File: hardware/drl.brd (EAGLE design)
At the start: 60.6 x 32.4 mm, 17 parts, among them IC1 TINY13-20SU, IC3 REG1117, Q1 IRF3205Z, Q2 IRF3205Z, T1 BC817-40, X1 CON1, X2 CON2

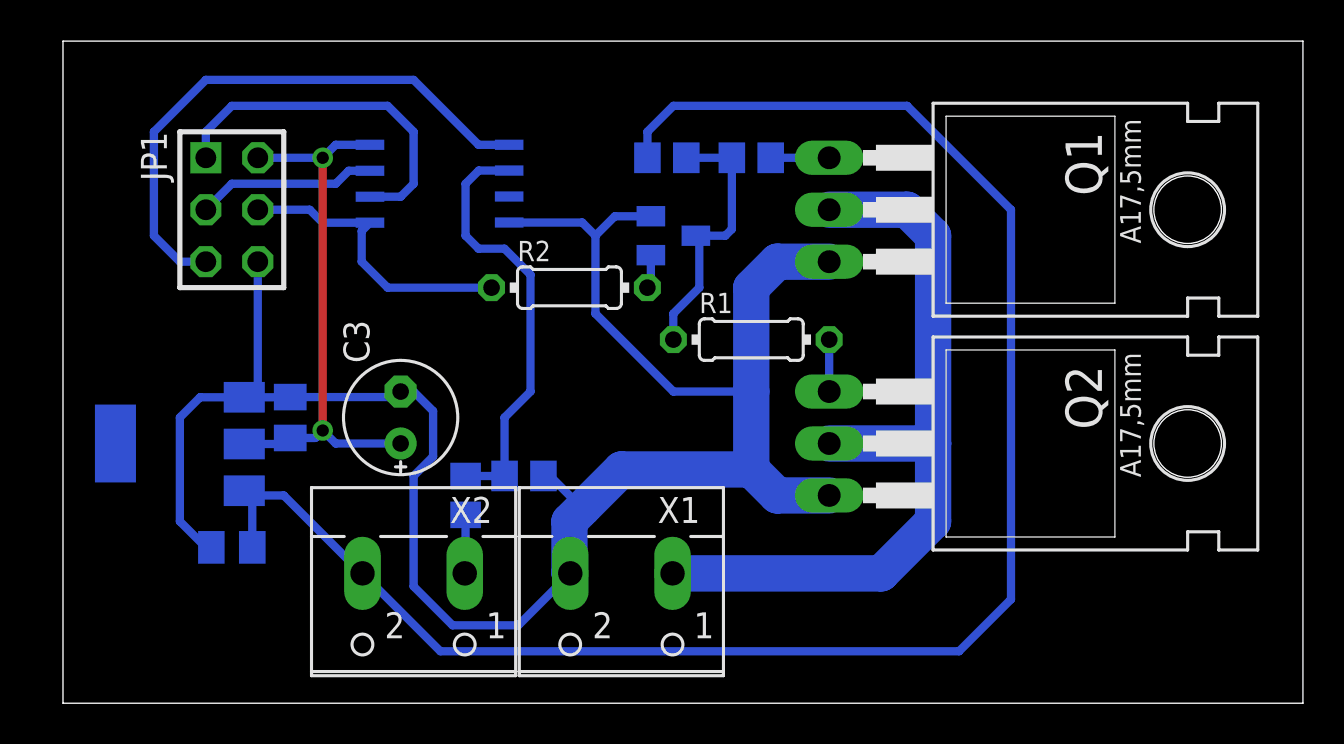
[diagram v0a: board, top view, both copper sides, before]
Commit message: Made the board slightly shorter. More compact component placement.
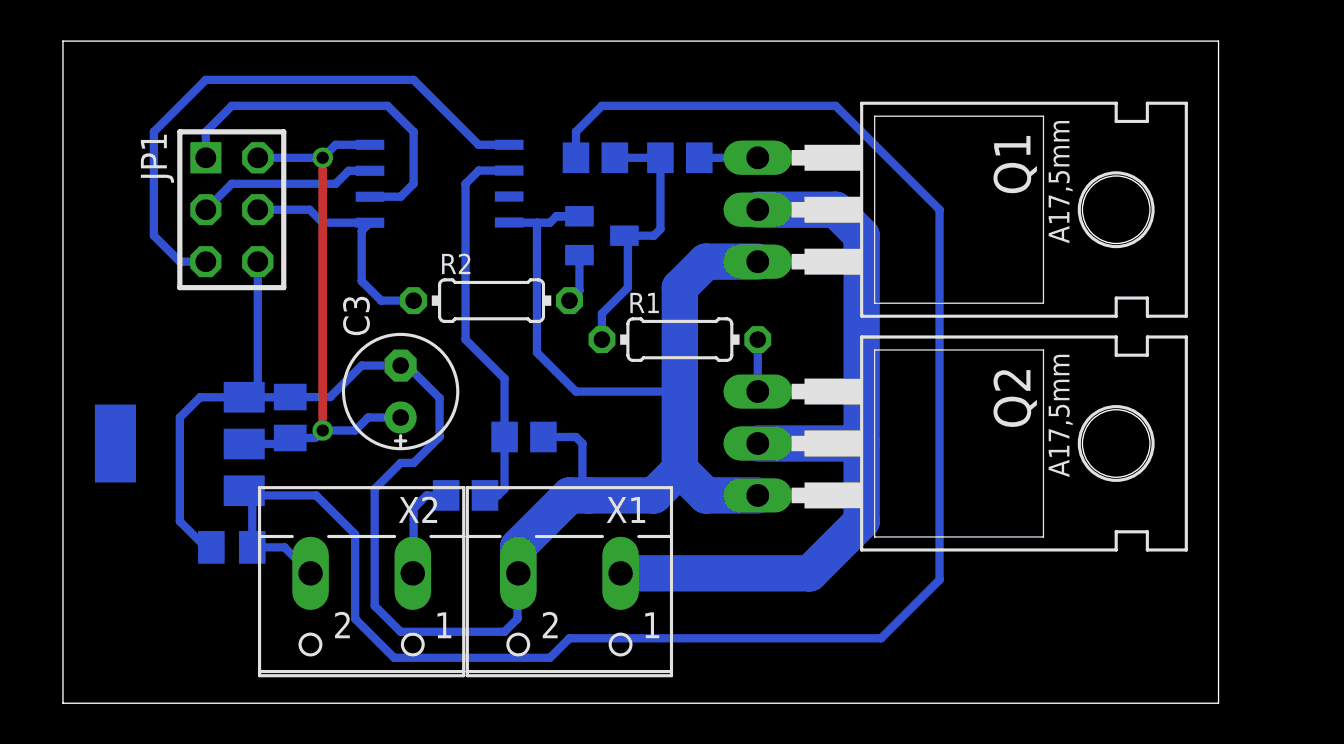
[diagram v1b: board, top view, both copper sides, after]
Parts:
- moved R2 3.86 mm to (21.0, 19.7)
- moved Q1 3.49 mm to (40.3, 24.1)
- moved Q2 3.49 mm to (40.3, 12.7)
- moved R1 3.49 mm to (30.2, 17.8)
- moved R3 3.49 mm to (30.2, 26.7)
- moved R4 3.49 mm to (26.0, 26.7)
- moved T1 3.49 mm to (26.4, 22.9)
- moved X1 2.54 mm to (24.8, 5.08)
- moved X2 2.54 mm to (14.6, 5.08)
- moved R7 1.90 mm to (22.5, 13.0)
- moved C3 1.27 mm to (16.5, 15.2)
- turned R6 to 0 degrees
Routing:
- net N$7: track 14.7 -> 11.7 mm
- net GND: track 99.2 -> 101.9 mm
- net LO_BEAM: track 2.88 -> 5.04 mm
- net +12: track 85.0 -> 87.0 mm
- net N$9: track 21.2 -> 19.2 mm
- net HI_BEAM: track 38.4 -> 37.5 mm
- net N$6: track 1.66 -> 2.43 mm
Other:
- board size 60.6 x 32.4 mm -> 56.5 x 32.4 mm

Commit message: Added ground plane
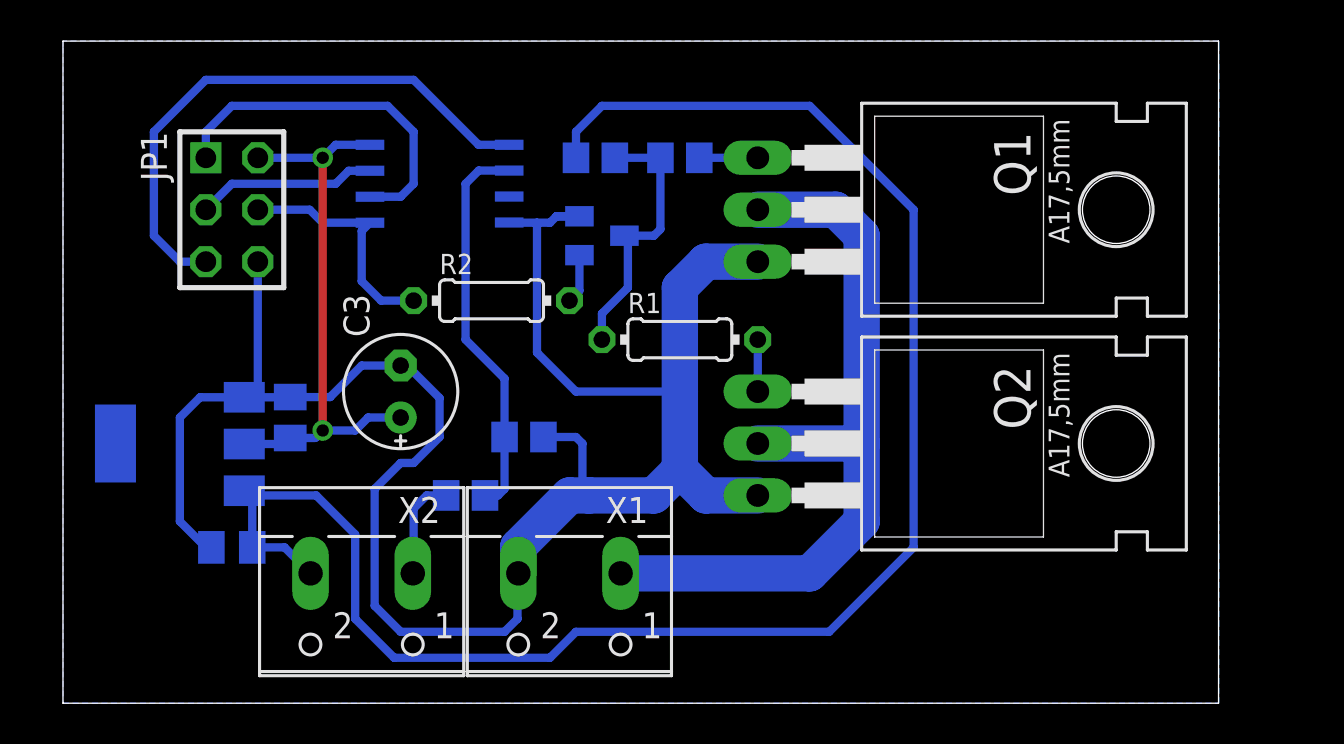
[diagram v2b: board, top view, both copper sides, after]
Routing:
- net +12: track 87.0 -> 83.6 mm
- added copper zone on layer 16, net N$2
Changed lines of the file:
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@@
 <wire x1="25.085" y1="26.67" x2="25.085" y2="27.9425" width="0.4064" layer="16"/>
 <wire x1="25.085" y1="27.9425" x2="26.3525" y2="29.21" width="0.4064" layer="16"/>
-<wire x1="26.3525" y1="29.21" x2="37.7825" y2="29.21" width="0.4064" layer="16"/>
-<wire x1="37.7825" y1="29.21" x2="42.8625" y2="24.13" width="0.4064" layer="16"/>
 <wire x1="9.255" y1="7.62" x2="10.835" y2="7.62" width="0.4064" layer="16"/>
 <wire x1="10.835" y1="7.62" x2="12.105" y2="6.35" width="0.4064" layer="16"/>
-<wire x1="40.005" y1="3.175" x2="42.8625" y2="6.0325" width="0.4064" layer="16"/>
-<wire x1="42.8625" y1="6.0325" x2="42.8625" y2="24.13" width="0.4064" layer="16"/>
 <wire x1="12.3825" y1="10.16" x2="14.2875" y2="8.255" width="0.4064" layer="16"/>
 <wire x1="14.2875" y1="8.255" x2="14.2875" y2="4.1275" width="0.4064" layer="16"/>
 <wire x1="14.2875" y1="4.1275" x2="16.1925" y2="2.2225" width="0.4064" layer="16"/>
 <wire x1="16.1925" y1="2.2225" x2="23.8125" y2="2.2225" width="0.4064" layer="16"/>
-<wire x1="23.8125" y1="2.2225" x2="24.765" y2="3.175" width="0.4064" layer="16"/>
-<wire x1="24.765" y1="3.175" x2="40.005" y2="3.175" width="0.4064" layer="16"/>
+<wire x1="23.8125" y1="2.2225" x2="25.0825" y2="3.4925" width="0.4064" layer="16"/>
+<wire x1="26.3525" y1="29.21" x2="36.5125" y2="29.21" width="0.4064" layer="16"/>
+<wire x1="36.5125" y1="29.21" x2="41.5925" y2="24.13" width="0.4064" layer="16"/>
+<wire x1="41.5925" y1="24.13" x2="41.5925" y2="7.62" width="0.4064" layer="16"/>
+<wire x1="41.5925" y1="7.62" x2="37.465" y2="3.4925" width="0.4064" layer="16"/>
+<wire x1="37.465" y1="3.4925" x2="25.0825" y2="3.4925" width="0.4064" layer="16"/>
 </signal>
 <signal name="N$4">
@@
 <wire x1="17.145" y1="6.39" x2="17.105" y2="6.35" width="0.4064" layer="16"/>
 </signal>
+<signal name="N$2">
+<polygon width="0.4064" layer="16" isolate="0.8128">
+<vertex x="0" y="0"/>
+<vertex x="56.515" y="0"/>
+<vertex x="56.515" y="32.0675"/>
+<vertex x="56.515" y="32.385"/>
+<vertex x="0" y="32.385"/>
+<vertex x="0" y="32.0675"/>
+</polygon>
+</signal>
 </signals>

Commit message: Change in schematic and board.
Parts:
- added C4: 47u, rcl:E2,5-6E
- added D1: (no value), semicon-smd-ipc:SOD80
- added R5: 10k, rcl:R0805
- C3: value 22u -> 100u
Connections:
- new net VCC12: C1.1, C4.+, D1.1, IC3.3, R4.2
- net +12: now also D1.2; no longer C1.1, IC3.3, R4.2
- net GND: now also C4.-
- net N$7: now also R5.2
- net VCC: now also R5.1
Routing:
- net VCC12: track 0.00 -> 87.5 mm
- net +12: track 83.6 -> 3.30 mm
- net N$7: track 11.7 -> 5.75 mm
- net GND: track 101.9 -> 105.3 mm
- added copper zone on layer 16, net GND
- removed copper zone on layer 16, net N$2
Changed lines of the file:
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@@
 <element name="C1" library="resistor" package="C0805K" value="100n" x="8.255" y="7.62" rot="MR0"/>
 <element name="C2" library="resistor" package="C0805K" value="100n" x="11.1125" y="13.97" rot="MR90"/>
-<element name="C3" library="rcl" package="E2,5-6E" value="22u" x="16.51" y="15.24" rot="R90"/>
+<element name="C3" library="rcl" package="E2,5-6E" value="100u" x="16.51" y="15.24" rot="R90"/>
 <element name="IC3" library="burr-brown" package="SOT223" value="REG1117" x="5.715" y="12.7" rot="MR270">
 <attribute name="OC_NEWARK" value="14P6981" x="5.715" y="12.7" size="1.778" layer="28" rot="MR270" display="off"/>
@@
 <element name="R1" library="rcl" package="0204/7" value="100" x="30.1625" y="17.78"/>
 <element name="R2" library="rcl" package="0204/7" value="1k" x="20.955" y="19.685"/>
+<element name="C4" library="rcl" package="E2,5-6E" value="47u" x="4.445" y="6.0325" rot="R180"/>
+<element name="D1" library="semicon-smd-ipc" package="SOD80" value="" x="8.5725" y="3.81" rot="MR180"/>
+<element name="R5" library="rcl" package="R0805" value="10k" x="14.605" y="20.0025" rot="MR90"/>
 </elements>
 <signals>
@@
 <wire x1="33.9725" y1="21.59" x2="31.4325" y2="21.59" width="1.778" layer="16"/>
 <wire x1="31.4325" y1="21.59" x2="30.1625" y2="20.32" width="1.778" layer="16"/>
-<wire x1="30.1625" y1="20.32" x2="30.1625" y2="15.24" width="1.778" layer="16"/>
-<wire x1="30.1625" y1="15.24" x2="30.1625" y2="11.43" width="1.778" layer="16"/>
+<wire x1="30.1625" y1="20.32" x2="30.1625" y2="11.43" width="1.778" layer="16"/>
 <wire x1="8.8646" y1="14.9606" x2="9.525" y2="14.9606" width="0.4064" layer="16"/>
 <wire x1="8.8646" y1="14.9606" x2="6.7056" y2="14.9606" width="0.4064" layer="16"/>
@@
 <wire x1="6.985" y1="7.62" x2="7.255" y2="7.62" width="0.4064" layer="16"/>
 <wire x1="9.525" y1="21.59" x2="9.525" y2="14.9606" width="0.4064" layer="16"/>
-<wire x1="25.0825" y1="15.24" x2="30.1625" y2="15.24" width="0.4064" layer="16"/>
 <wire x1="9.525" y1="14.9606" x2="10.7856" y2="14.9606" width="0.4064" layer="16"/>
 <wire x1="10.7856" y1="14.9606" x2="11.1125" y2="14.97" width="0.4064" layer="16"/>
@@
 <wire x1="25.7175" y1="10.16" x2="28.8925" y2="10.16" width="1.778" layer="16"/>
 <wire x1="28.8925" y1="10.16" x2="30.1625" y2="11.43" width="1.778" layer="16"/>
-<wire x1="23.4925" y1="13.0175" x2="25.0825" y2="13.0175" width="0.4064" layer="16"/>
-<wire x1="25.0825" y1="13.0175" x2="25.4" y2="12.7" width="0.4064" layer="16"/>
-<wire x1="25.4" y1="12.7" x2="25.4" y2="10.4775" width="0.4064" layer="16"/>
 <wire x1="25.4" y1="10.4775" x2="25.7175" y2="10.16" width="0.4064" layer="16"/>
 <wire x1="11.1125" y1="14.97" x2="13.065" y2="14.97" width="0.4064" layer="16"/>
@@
 <wire x1="23.8125" y1="23.495" x2="23.1775" y2="23.495" width="0.4064" layer="16"/>
 <wire x1="23.1775" y1="23.495" x2="23.1775" y2="17.145" width="0.4064" layer="16"/>
-<wire x1="23.1775" y1="17.145" x2="25.0825" y2="15.24" width="0.4064" layer="16"/>
+<contactref element="C4" pad="-"/>
+<wire x1="23.1775" y1="17.145" x2="23.4925" y2="16.83" width="0.4064" layer="16"/>
+<wire x1="23.4925" y1="16.83" x2="23.4925" y2="13.0175" width="0.4064" layer="16"/>
+<wire x1="23.4925" y1="13.0175" x2="23.495" y2="13.02" width="0.4064" layer="16"/>
+<wire x1="23.495" y1="13.02" x2="23.495" y2="17.145" width="0.4064" layer="16"/>
+<wire x1="23.495" y1="17.145" x2="23.1775" y2="17.4625" width="0.4064" layer="16"/>
+<wire x1="18.0975" y1="17.4625" x2="17.4625" y2="17.4625" width="0.4064" layer="16"/>
+<wire x1="17.4625" y1="17.4625" x2="16.51" y2="16.51" width="0.4064" layer="16"/>
+<wire x1="3.175" y1="6.0325" x2="3.175" y2="7.62" width="0.4064" layer="16"/>
+<wire x1="3.175" y1="7.62" x2="4.445" y2="8.89" width="0.4064" layer="16"/>
+<wire x1="4.445" y1="8.89" x2="5.715" y2="8.89" width="0.4064" layer="16"/>
+<polygon width="0.4064" layer="16" isolate="0.8128">
+<vertex x="0" y="0"/>
+<vertex x="56.515" y="0"/>
+<vertex x="56.515" y="32.0675"/>
+<vertex x="56.515" y="32.385"/>
+<vertex x="0" y="32.385"/>
+<vertex x="0" y="32.0675"/>
+</polygon>
 </signal>
 <signal name="HI_BEAM">
@@
 <wire x1="12.065" y1="24.13" x2="9.525" y2="24.13" width="0.4064" layer="16"/>
 <contactref element="R2" pad="1"/>
-<wire x1="14.605" y1="20.6375" x2="14.605" y2="23.089" width="0.4064" layer="16"/>
-<wire x1="14.605" y1="23.089" x2="15.011" y2="23.495" width="0.4064" layer="16"/>
-<wire x1="14.605" y1="20.6375" x2="15.5575" y2="19.685" width="0.4064" layer="16"/>
-<wire x1="15.5575" y1="19.685" x2="17.145" y2="19.685" width="0.4064" layer="16"/>
+<wire x1="14.605" y1="20.6375" x2="14.605" y2="23.089" width="0" layer="19" extent="1-16"/>
+<wire x1="14.605" y1="23.089" x2="15.011" y2="23.495" width="0" layer="19" extent="1-16"/>
+<wire x1="14.605" y1="20.6375" x2="15.5575" y2="19.685" width="0" layer="19" extent="1-16"/>
+<wire x1="15.5575" y1="19.685" x2="17.145" y2="19.685" width="0" layer="19" extent="1-16"/>
+<contactref element="R5" pad="2"/>
+<wire x1="14.605" y1="20.9525" x2="15.5575" y2="19.685" width="0" layer="19" extent="1-16"/>
 </signal>
 <signal name="N$8">
@@
 </signal>
 <signal name="+12">
-<contactref element="R4" pad="2"/>
-<contactref element="C1" pad="1"/>
-<contactref element="IC3" pad="3"/>
-<wire x1="9.255" y1="7.62" x2="9.255" y2="9.9982" width="0.4064" layer="16"/>
-<wire x1="9.255" y1="9.9982" x2="8.8646" y2="10.3886" width="0.4064" layer="16"/>
 <contactref element="X2" pad="2"/>
-<wire x1="12.3825" y1="10.16" x2="9.4168" y2="10.16" width="0.4064" layer="16"/>
-<wire x1="9.4168" y1="10.16" x2="9.255" y2="9.9982" width="0.4064" layer="16"/>
-<wire x1="25.085" y1="26.67" x2="25.085" y2="27.9425" width="0.4064" layer="16"/>
-<wire x1="25.085" y1="27.9425" x2="26.3525" y2="29.21" width="0.4064" layer="16"/>
-<wire x1="9.255" y1="7.62" x2="10.835" y2="7.62" width="0.4064" layer="16"/>
-<wire x1="10.835" y1="7.62" x2="12.105" y2="6.35" width="0.4064" layer="16"/>
-<wire x1="12.3825" y1="10.16" x2="14.2875" y2="8.255" width="0.4064" layer="16"/>
-<wire x1="14.2875" y1="8.255" x2="14.2875" y2="4.1275" width="0.4064" layer="16"/>
-<wire x1="14.2875" y1="4.1275" x2="16.1925" y2="2.2225" width="0.4064" layer="16"/>
-<wire x1="16.1925" y1="2.2225" x2="23.8125" y2="2.2225" width="0.4064" layer="16"/>
-<wire x1="23.8125" y1="2.2225" x2="25.0825" y2="3.4925" width="0.4064" layer="16"/>
-<wire x1="26.3525" y1="29.21" x2="36.5125" y2="29.21" width="0.4064" layer="16"/>
-<wire x1="36.5125" y1="29.21" x2="41.5925" y2="24.13" width="0.4064" layer="16"/>
-<wire x1="41.5925" y1="24.13" x2="41.5925" y2="7.62" width="0.4064" layer="16"/>
-<wire x1="41.5925" y1="7.62" x2="37.465" y2="3.4925" width="0.4064" layer="16"/>
-<wire x1="37.465" y1="3.4925" x2="25.0825" y2="3.4925" width="0.4064" layer="16"/>
+<contactref element="D1" pad="2"/>
+<wire x1="12.105" y1="6.35" x2="12.105" y2="5.6425" width="0.4064" layer="16"/>
+<wire x1="12.105" y1="5.6425" x2="10.2725" y2="3.81" width="0.4064" layer="16"/>
 </signal>
 <signal name="N$4">
@@
 <wire x1="14.9225" y1="13.97" x2="14.2875" y2="13.335" width="0.4064" layer="16"/>
 <wire x1="14.2875" y1="13.335" x2="12.7" y2="13.335" width="0.4064" layer="16"/>
+<contactref element="R5" pad="1"/>
+<wire x1="14.605" y1="19.0525" x2="8.8646" y2="12.6746" width="0" layer="19" extent="1-16"/>
 </signal>
 <signal name="N$9">
@@
 <wire x1="17.145" y1="6.39" x2="17.105" y2="6.35" width="0.4064" layer="16"/>
 </signal>
-<signal name="N$2">
-<polygon width="0.4064" layer="16" isolate="0.8128">
-<vertex x="0" y="0"/>
-<vertex x="56.515" y="0"/>
-<vertex x="56.515" y="32.0675"/>
-<vertex x="56.515" y="32.385"/>
-<vertex x="0" y="32.385"/>
-<vertex x="0" y="32.0675"/>
-</polygon>
+<signal name="VCC12">
+<contactref element="C1" pad="1"/>
+<contactref element="IC3" pad="3"/>
+<contactref element="C4" pad="+"/>
+<contactref element="D1" pad="1"/>
+<contactref element="R4" pad="2"/>
+<wire x1="9.255" y1="7.62" x2="9.255" y2="9.9982" width="0.4064" layer="16"/>
+<wire x1="9.255" y1="9.9982" x2="8.8646" y2="10.3886" width="0.4064" layer="16"/>
+<wire x1="12.3825" y1="10.16" x2="9.4168" y2="10.16" width="0.4064" layer="16"/>
+<wire x1="9.4168" y1="10.16" x2="9.255" y2="9.9982" width="0.4064" layer="16"/>
+<wire x1="25.085" y1="27.9425" x2="26.3525" y2="29.21" width="0.4064" layer="16"/>
+<wire x1="12.3825" y1="10.16" x2="14.2875" y2="8.255" width="0.4064" layer="16"/>
+<wire x1="14.2875" y1="8.255" x2="14.2875" y2="4.1275" width="0.4064" layer="16"/>
+<wire x1="14.2875" y1="4.1275" x2="16.1925" y2="2.2225" width="0.4064" layer="16"/>
+<wire x1="16.1925" y1="2.2225" x2="23.8125" y2="2.2225" width="0.4064" layer="16"/>
+<wire x1="23.8125" y1="2.2225" x2="25.0825" y2="3.4925" width="0.4064" layer="16"/>
+<wire x1="26.3525" y1="29.21" x2="36.5125" y2="29.21" width="0.4064" layer="16"/>
+<wire x1="36.5125" y1="29.21" x2="41.5925" y2="24.13" width="0.4064" layer="16"/>
+<wire x1="41.5925" y1="24.13" x2="41.5925" y2="7.62" width="0.4064" layer="16"/>
+<wire x1="41.5925" y1="7.62" x2="37.465" y2="3.4925" width="0.4064" layer="16"/>
+<wire x1="37.465" y1="3.4925" x2="25.0825" y2="3.4925" width="0.4064" layer="16"/>
+<wire x1="6.8725" y1="3.81" x2="6.8725" y2="4.875" width="0.4064" layer="16"/>
+<wire x1="6.8725" y1="4.875" x2="5.715" y2="6.0325" width="0.4064" layer="16"/>
+<wire x1="6.8725" y1="4.875" x2="8.3675" y2="4.875" width="0.4064" layer="16"/>
+<wire x1="8.3675" y1="4.875" x2="9.2075" y2="5.715" width="0.4064" layer="16"/>
+<wire x1="9.2075" y1="5.715" x2="9.2075" y2="7.5725" width="0.4064" layer="16"/>
+<wire x1="9.2075" y1="7.5725" x2="9.255" y2="7.62" width="0.4064" layer="16"/>
+<wire x1="25.085" y1="26.67" x2="25.085" y2="27.9425" width="0.4064" layer="16"/>
 </signal>
 </signals>

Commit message: Resistor value was edited
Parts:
- R6: value 30k -> 22k
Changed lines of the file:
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@@
 <attribute name="OC_FARNELL" value="1097566" x="5.715" y="12.7" size="1.778" layer="28" rot="MR270" display="off"/>
 </element>
-<element name="R6" library="rcl" package="R0805" value="30k" x="19.685" y="10.16" rot="MR0"/>
+<element name="R6" library="rcl" package="R0805" value="22k" x="19.685" y="10.16" rot="MR0"/>
 <element name="R7" library="rcl" package="R0805" value="10k" x="22.5425" y="13.0175" rot="MR0"/>
 <element name="X1" library="con-wago-500" package="W237-102" value="CON1" x="24.765" y="5.08" rot="R180">

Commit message: Second version of hardware (schematic and pcb)
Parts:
- removed IC3: REG1117, burr-brown:SOT223
- added C5, C6: 100n, resistor:C0805K
- added D2: (no value), semicon-smd-ipc:SOD80
- added IC2: (no value), my_stuff:SOIC8
- added R10, R8: 10k, rcl:R0805
- added R9: 22k, rcl:R0805
- added S1: (no value), switch-omron:B3F-10XX
- C3: value 100u -> 10u; device rcl:E2,5-6E -> rcl:SMC_D
- C4: value 47u -> 10u; device rcl:E2,5-6E -> rcl:SMC_D
- Q1, Q2: value IRF3205Z -> IRF3205; device my_stuff:TO220AB -> my_stuff:TO220BV
- R1: device rcl:0204/7 -> rcl:R0805
- moved X1 18.4 mm to (43.2, 5.40)
- moved X2 18.1 mm to (32.7, 5.40)
- moved C4 14.5 mm to (18.1, 10.8), flipped to the bottom, turned to 270 degrees
- moved R6 13.8 mm to (33.0, 13.7), turned to 270 degrees
- moved R7 13.3 mm to (34.9, 17.8), turned to 270 degrees
- moved C3 10.7 mm to (10.2, 6.67), flipped to the bottom
- moved T1 10.2 mm to (36.5, 23.8)
- moved R4 9.89 mm to (35.9, 27.6)
- moved R3 9.85 mm to (40.0, 26.4), turned to 270 degrees
- moved R1 8.64 mm to (38.4, 15.2), flipped to the bottom, turned to 270 degrees
- moved D1 6.98 mm to (15.6, 3.81)
- moved C1 5.41 mm to (13.7, 7.30), turned to 90 degrees
- moved C2 4.76 mm to (14.9, 16.8)
- moved Q2 4.58 mm to (42.9, 16.5), turned to 0 degrees
- moved IC1 4.46 mm to (22.9, 25.7)
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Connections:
- removed net LO_BEAM: R6.2, X2.1
- removed net N$5: IC1.6, JP1.1
- new net N$11: IC1.5, JP1.4, R2.1, R5.1
- new net N$12: IC1.6, JP1.1, S1.4
- new net N$14: C6.1, IC1.3, R8.1, R9.2
- new net N$2: D2.1, R6.2
- net GND: now also C5.2, C6.2, IC2.2, IC2.3, IC2.6, IC2.7, R8.2, S1.1, S1.2, X1.1; no longer IC3.1, X1.2
- net HI_BEAM: now also X1.2; no longer X1.1
- net N$10: now also R10.2
- net N$7: now also D2.2, X2.1; no longer IC1.5, JP1.4, R2.1, R5.2
- net N$9: now also C5.1
- net VCC: now also C4.+, IC2.1, R10.1, R5.2; no longer C3.+, IC3.2, R5.1
- net VCC12: now also C3.+, IC2.8, R9.1; no longer C4.+, IC3.3
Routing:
- net N$12: track 0.00 -> 24.1 mm
- net HI_BEAM: track 37.5 -> 14.9 mm
- net VCC12: track 87.5 -> 69.1 mm
- net N$5: track 17.4 -> 0.00 mm
- net GND: track 105.3 -> 88.8 mm, vias 0 -> 2
- net VCC: track 27.2 -> 39.7 mm
- net N$11: track 0.00 -> 12.3 mm
- net +12: track 3.30 -> 14.1 mm
- net N$9: track 19.2 -> 28.8 mm
- net N$14: track 0.00 -> 9.43 mm
- net N$6: track 2.43 -> 7.58 mm
- net LO_BEAM: track 5.04 -> 0.00 mm
- net N$7: track 5.75 -> 3.06 mm
- net N$8: track 13.3 -> 15.4 mm
- net N$3: track 2.86 -> 4.90 mm
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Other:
- board text added: "DRL v2"
